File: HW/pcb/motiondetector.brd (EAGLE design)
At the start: 100 x 80 mm, 1 part, among them IC1 4000D

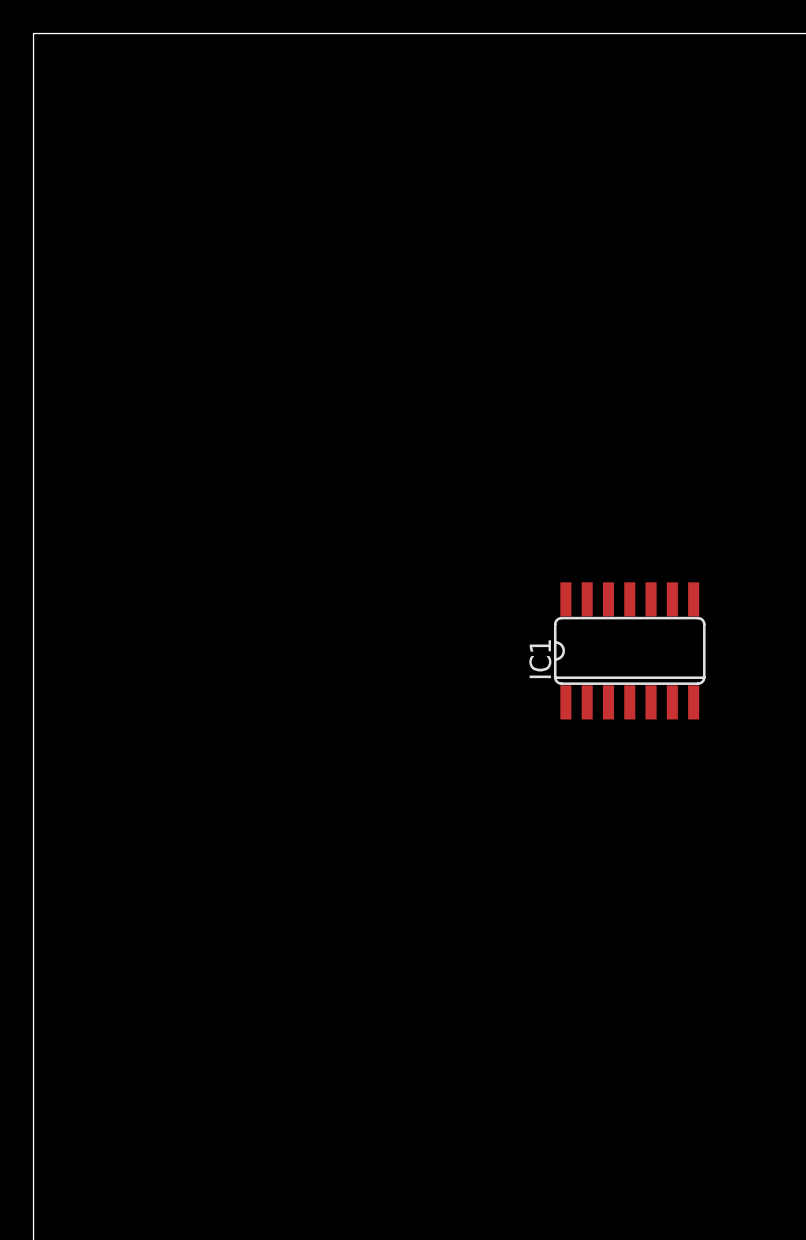
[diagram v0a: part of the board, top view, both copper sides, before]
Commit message: analog stage in circuit finished and testet
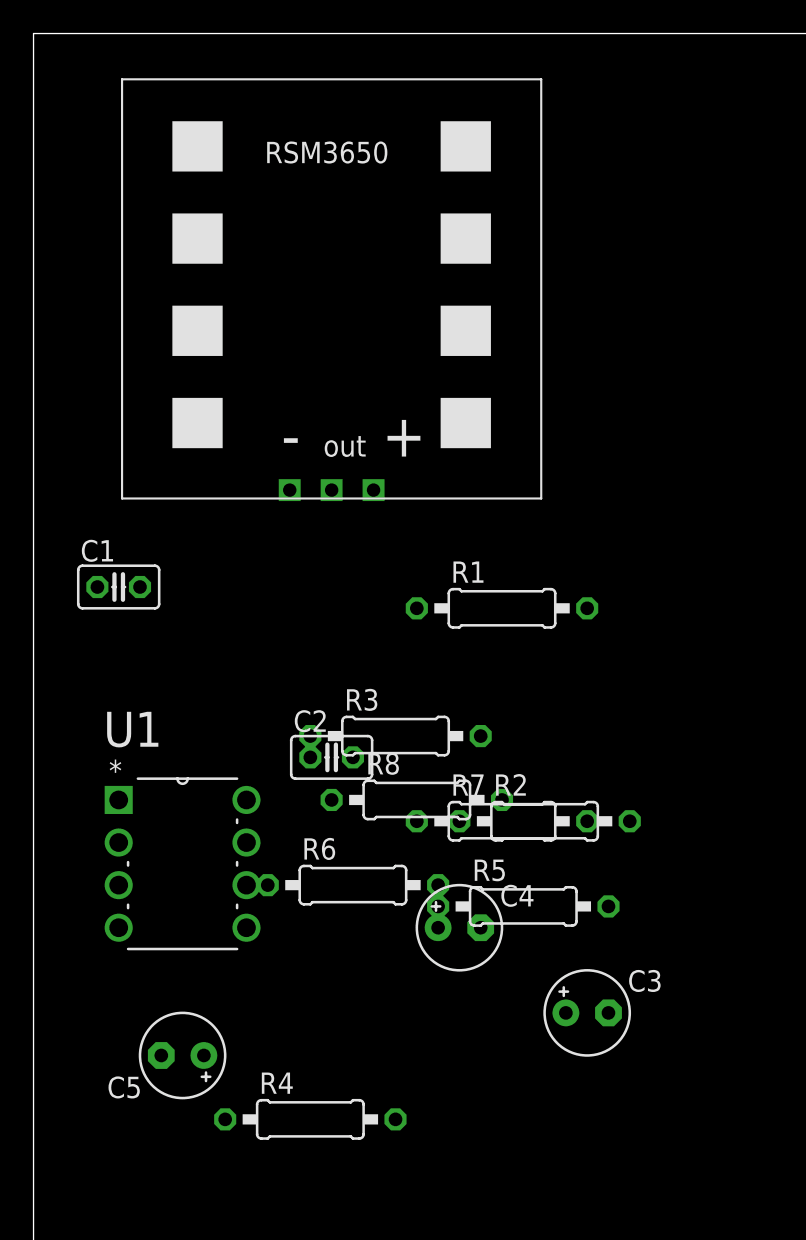
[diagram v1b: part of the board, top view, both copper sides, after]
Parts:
- removed IC1: 4000D, 40xx:SO14
- added C1, C2: 1nF, parts:C025-025X050
- added C3, C4, C5: 10uF, parts:E2,5-5
- added R1, R2: 4.7K, parts:0207/10
- added R3, R4: 1M, parts:0207/10
- added R5, R6: 1k, parts:0207/10
- added R7, R8: 150k, parts:0207/10
- added U$1: RSM3650, RSM3650:RSM3650
- added U1: LT1078CN8PBF, parts:DIP254P762X393-8
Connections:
- removed net VDD: IC1.14
- removed net VSS: IC1.7
- new net +3V3: R3.2, U$1.VCC, U1.8
- new net GND: C5.-, R4.1, U$1.VSS, U1.4
- new net N$1: C4.-, R1.1
- new net N$11: C2.1, R2.2, R8.1, U1.6
- new net N$2: C1.2, R1.2, R7.1, U1.2
- new net N$3: C4.+, U$1.OUT
- new net N$4: C3.-, R2.1
- new net N$5: R5.1
- new net N$6: R6.2, U1.3, U1.5
- new net N$7: C5.+, R3.1, R4.2, R6.1
- new net N$8: C2.2, R5.2, R8.2, U1.7
- new net N$9: C1.1, C3.+, R7.2, U1.1
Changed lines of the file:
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@@
 <layer number="97" name="Info" color="7" fill="1" visible="no" active="no"/>
 <layer number="98" name="Guide" color="6" fill="1" visible="no" active="no"/>
+<layer number="99" name="SpiceOrder" color="5" fill="1" visible="no" active="no"/>
 </layers>
 <board>
@@
 </autorouter>
 <elements>
-<element name="IC1" library="40xx" package="SO14" value="4000D" x="35.56" y="43.18"/>
+<element name="U1" library="parts" package="DIP254P762X393-8" value="LT1078CN8PBF" x="12.7" y="26.67">
+<attribute name="SUPPLIER" value="LINEAR TECHNOLOGY" x="12.7" y="26.67" size="1.778" layer="27" display="off"/>
+<attribute name="MPN" value="LT1078CN8#PBF" x="12.7" y="26.67" size="1.778" layer="27" display="off"/>
+<attribute name="OC_FARNELL" value="9559680" x="12.7" y="26.67" size="1.778" layer="27" display="off"/>
+<attribute name="OC_NEWARK" value="57M1404" x="12.7" y="26.67" size="1.778" layer="27" display="off"/>
+<attribute name="PACKAGE" value="PDIP" x="12.7" y="26.67" size="1.778" layer="27" display="off"/>
+</element>
+<element name="C1" library="parts" package="C025-025X050" value="1nF" x="5.08" y="46.99"/>
+<element name="C2" library="parts" package="C025-025X050" value="1nF" x="17.78" y="36.83"/>
+<element name="C3" library="parts" package="E2,5-5" value="10uF" x="33.02" y="21.59"/>
+<element name="C4" library="parts" package="E2,5-5" value="10uF" x="25.4" y="26.67"/>
+<element name="C5" library="parts" package="E2,5-5" value="10uF" x="8.89" y="19.05" rot="R180"/>
+<element name="R1" library="parts" package="0207/10" value="4.7K" x="27.94" y="45.72"/>
+<element name="R2" library="parts" package="0207/10" value="4.7K" x="30.48" y="33.02"/>
+<element name="R3" library="parts" package="0207/10" value="1M" x="21.59" y="38.1"/>
+<element name="R4" library="parts" package="0207/10" value="1M" x="16.51" y="15.24"/>
+<element name="R5" library="parts" package="0207/10" value="1k" x="29.21" y="27.94"/>
+<element name="R6" library="parts" package="0207/10" value="1k" x="19.05" y="29.21"/>
+<element name="R7" library="parts" package="0207/10" value="150k" x="27.94" y="33.02"/>
+<element name="R8" library="parts" package="0207/10" value="150k" x="22.86" y="34.29"/>
+<element name="U$1" library="RSM3650" package="RSM3650" value="RSM3650" x="17.78" y="64.77"/>
 </elements>
 <signals>
-<signal name="VSS">
-<contactref element="IC1" pad="7"/>
-</signal>
-<signal name="VDD">
-<contactref element="IC1" pad="14"/>
+<signal name="+3V3">
+<contactref element="U1" pad="8"/>
+<contactref element="R3" pad="2"/>
+<contactref element="U$1" pad="VCC"/>
+<wire x1="12.7" y1="34.29" x2="26.67" y2="38.1" width="0" layer="19" extent="1-1"/>
+<wire x1="20.28" y1="52.77" x2="12.7" y2="34.29" width="0" layer="19" extent="1-1"/>
+</signal>
+<signal name="N$1">
+<contactref element="C4" pad="-"/>
+<contactref element="R1" pad="1"/>
+<wire x1="26.67" y1="26.67" x2="22.86" y2="45.72" width="0" layer="19" extent="1-1"/>
+</signal>
+<signal name="N$2">
+<contactref element="R1" pad="2"/>
+<contactref element="U1" pad="2"/>
+<contactref element="R7" pad="1"/>
+<contactref element="C1" pad="2"/>
+<wire x1="33.02" y1="45.72" x2="22.86" y2="33.02" width="0" layer="19" extent="1-1"/>
+<wire x1="6.35" y1="46.99" x2="33.02" y2="45.72" width="0" layer="19" extent="1-1"/>
+<wire x1="5.08" y1="31.75" x2="6.35" y2="46.99" width="0" layer="19" extent="1-1"/>
+</signal>
+<signal name="N$4">
+<contactref element="C3" pad="-"/>
+<contactref element="R2" pad="1"/>
+<wire x1="34.29" y1="21.59" x2="25.4" y2="33.02" width="0" layer="19" extent="1-1"/>
+</signal>
+<signal name="N$6">
+<contactref element="U1" pad="3"/>
+<contactref element="U1" pad="5"/>
+<contactref element="R6" pad="2"/>
+<wire x1="12.7" y1="26.67" x2="24.13" y2="29.21" width="0" layer="19" extent="1-1"/>
+<wire x1="5.08" y1="29.21" x2="12.7" y2="26.67" width="0" layer="19" extent="1-1"/>
+</signal>
+<signal name="N$7">
+<contactref element="R3" pad="1"/>
+<contactref element="R4" pad="2"/>
+<contactref element="C5" pad="+"/>
+<contactref element="R6" pad="1"/>
+<wire x1="21.59" y1="15.24" x2="13.97" y2="29.21" width="0" layer="19" extent="1-1"/>
+<wire x1="16.51" y1="38.1" x2="21.59" y2="15.24" width="0" layer="19" extent="1-1"/>
+<wire x1="10.16" y1="19.05" x2="16.51" y2="38.1" width="0" layer="19" extent="1-1"/>
+</signal>
+<signal name="N$9">
+<contactref element="C1" pad="1"/>
+<contactref element="R7" pad="2"/>
+<contactref element="U1" pad="1"/>
+<contactref element="C3" pad="+"/>
+<wire x1="31.75" y1="21.59" x2="33.02" y2="33.02" width="0" layer="19" extent="1-1"/>
+<wire x1="3.81" y1="46.99" x2="31.75" y2="21.59" width="0" layer="19" extent="1-1"/>
+<wire x1="5.08" y1="34.29" x2="3.81" y2="46.99" width="0" layer="19" extent="1-1"/>
+</signal>
+<signal name="N$5">
+<contactref element="R5" pad="1"/>
+</signal>
+<signal name="GND">
+<contactref element="C5" pad="-"/>
+<contactref element="U1" pad="4"/>
+<contactref element="R4" pad="1"/>
+<contactref element="U$1" pad="VSS"/>
+<wire x1="7.62" y1="19.05" x2="11.43" y2="15.24" width="0" layer="19" extent="1-1"/>
+<wire x1="5.08" y1="26.67" x2="7.62" y2="19.05" width="0" layer="19" extent="1-1"/>
+<wire x1="15.28" y1="52.77" x2="5.08" y2="26.67" width="0" layer="19" extent="1-1"/>
+</signal>
+<signal name="N$8">
+<contactref element="R8" pad="2"/>
+<contactref element="C2" pad="2"/>
+<contactref element="U1" pad="7"/>
+<contactref element="R5" pad="2"/>
+<wire x1="34.29" y1="27.94" x2="27.94" y2="34.29" width="0" layer="19" extent="1-1"/>
+<wire x1="19.05" y1="36.83" x2="34.29" y2="27.94" width="0" layer="19" extent="1-1"/>
+<wire x1="12.7" y1="31.75" x2="19.05" y2="36.83" width="0" layer="19" extent="1-1"/>
+</signal>
+<signal name="N$11">
+<contactref element="R8" pad="1"/>
+<contactref element="C2" pad="1"/>
+<contactref element="R2" pad="2"/>
+<contactref element="U1" pad="6"/>
+<wire x1="35.56" y1="33.02" x2="17.78" y2="34.29" width="0" layer="19" extent="1-1"/>
+<wire x1="16.51" y1="36.83" x2="35.56" y2="33.02" width="0" layer="19" extent="1-1"/>
+<wire x1="12.7" y1="29.21" x2="16.51" y2="36.83" width="0" layer="19" extent="1-1"/>
+</signal>
+<signal name="N$3">
+<contactref element="U$1" pad="OUT"/>
+<contactref element="C4" pad="+"/>
+<wire x1="17.78" y1="52.77" x2="24.13" y2="26.67" width="0" layer="19" extent="1-1"/>
 </signal>
 </signals>

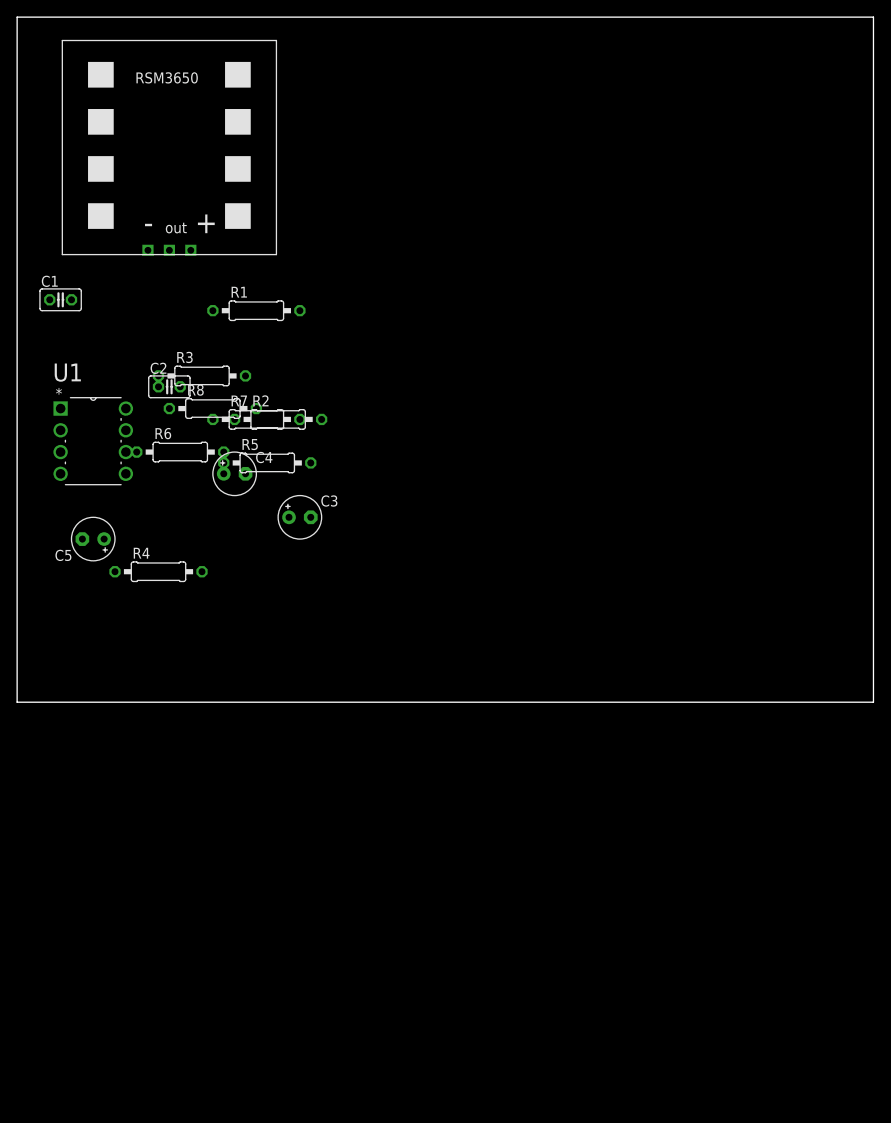
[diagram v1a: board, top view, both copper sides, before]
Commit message: base PIC24F circuit added
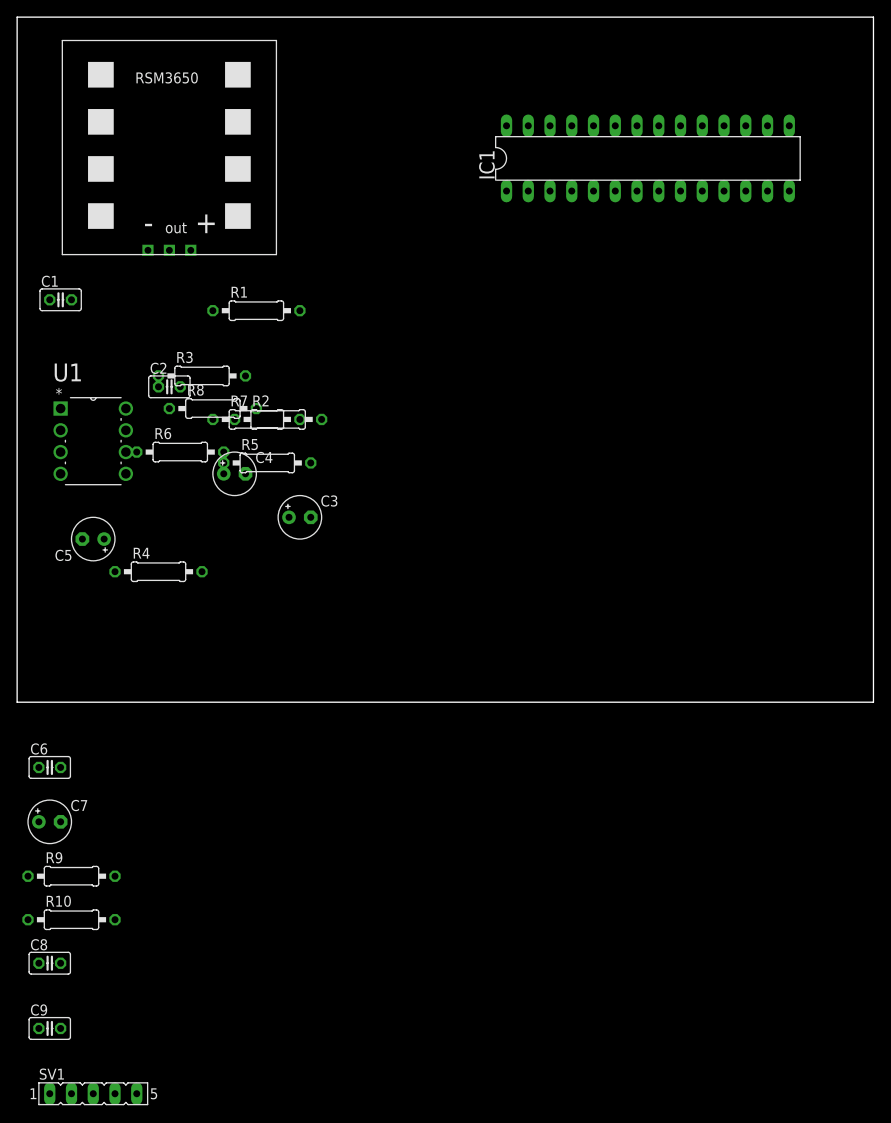
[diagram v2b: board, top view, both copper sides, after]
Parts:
- added C6, C8, C9: 100nF, parts:C025-025X050
- added C7: 10uF, parts:E2,5-5
- added IC1: PIC24FJ32GB002, PIC24FJXXGB0XX :DIL28-3
- added R10: 100R, parts:0207/10
- added R9: 10k, parts:0207/10
- added SV1: (no value), con-lsta:FE05-1
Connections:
- net N$5 renamed ROUT
- new net MCLR: C9.2, R10.2, R9.2, SV1.1
- new net N$12: C7.+, IC1.20
- new net N$13: IC1.1, R10.1
- new net PGEC1: IC1.5, SV1.5
- new net PGED1: IC1.4, SV1.4
- net +3V3: now also C6.2, C8.1, IC1.13, IC1.28, R9.1, SV1.2
- net GND: now also C6.1, C7.-, C8.2, C9.1, IC1.19, IC1.27, IC1.8, SV1.3
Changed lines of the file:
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@@
 <element name="R8" library="parts" package="0207/10" value="150k" x="22.86" y="34.29"/>
 <element name="U$1" library="RSM3650" package="RSM3650" value="RSM3650" x="17.78" y="64.77"/>
+<element name="IC1" library="PIC24FJXXGB0XX " package="DIL28-3" value="PIC24FJ32GB002" x="73.66" y="63.5"/>
+<element name="C6" library="parts" package="C025-025X050" value="100nF" x="3.81" y="-7.62"/>
+<element name="C7" library="parts" package="E2,5-5" value="10uF" x="3.81" y="-13.97"/>
+<element name="R9" library="parts" package="0207/10" value="10k" x="6.35" y="-20.32"/>
+<element name="R10" library="parts" package="0207/10" value="100R" x="6.35" y="-25.4"/>
+<element name="C8" library="parts" package="C025-025X050" value="100nF" x="3.81" y="-30.48"/>
+<element name="C9" library="parts" package="C025-025X050" value="100nF" x="3.81" y="-38.1"/>
+<element name="SV1" library="con-lsta" package="FE05-1" value="" x="8.89" y="-45.72">
+<attribute name="MPN" value="" x="8.89" y="-45.72" size="1.778" layer="27" display="off"/>
+<attribute name="MF" value="" x="8.89" y="-45.72" size="1.778" layer="27" display="off"/>
+<attribute name="OC_NEWARK" value="unknown" x="8.89" y="-45.72" size="1.778" layer="27" display="off"/>
+<attribute name="OC_FARNELL" value="unknown" x="8.89" y="-45.72" size="1.778" layer="27" display="off"/>
+</element>
 </elements>
 <signals>
@@
 <contactref element="R3" pad="2"/>
 <contactref element="U$1" pad="VCC"/>
+<contactref element="IC1" pad="28"/>
+<contactref element="C6" pad="2"/>
+<contactref element="R9" pad="1"/>
+<contactref element="IC1" pad="13"/>
+<contactref element="C8" pad="1"/>
+<contactref element="SV1" pad="2"/>
+<wire x1="57.15" y1="67.31" x2="87.63" y2="59.69" width="0" layer="19" extent="1-1"/>
+<wire x1="20.28" y1="52.77" x2="57.15" y2="67.31" width="0" layer="19" extent="1-1"/>
+<wire x1="26.67" y1="38.1" x2="20.28" y2="52.77" width="0" layer="19" extent="1-1"/>
 <wire x1="12.7" y1="34.29" x2="26.67" y2="38.1" width="0" layer="19" extent="1-1"/>
-<wire x1="20.28" y1="52.77" x2="12.7" y2="34.29" width="0" layer="19" extent="1-1"/>
+<wire x1="5.08" y1="-7.62" x2="12.7" y2="34.29" width="0" layer="19" extent="1-1"/>
+<wire x1="1.27" y1="-20.32" x2="5.08" y2="-7.62" width="0" layer="19" extent="1-1"/>
+<wire x1="2.54" y1="-30.48" x2="1.27" y2="-20.32" width="0" layer="19" extent="1-1"/>
+<wire x1="6.35" y1="-45.72" x2="2.54" y2="-30.48" width="0" layer="19" extent="1-1"/>
 </signal>
 <signal name="N$1">
@@
 <wire x1="5.08" y1="34.29" x2="3.81" y2="46.99" width="0" layer="19" extent="1-1"/>
 </signal>
-<signal name="N$5">
-<contactref element="R5" pad="1"/>
-</signal>
 <signal name="GND">
 <contactref element="C5" pad="-"/>
@@
 <contactref element="R4" pad="1"/>
 <contactref element="U$1" pad="VSS"/>
-<wire x1="7.62" y1="19.05" x2="11.43" y2="15.24" width="0" layer="19" extent="1-1"/>
-<wire x1="5.08" y1="26.67" x2="7.62" y2="19.05" width="0" layer="19" extent="1-1"/>
-<wire x1="15.28" y1="52.77" x2="5.08" y2="26.67" width="0" layer="19" extent="1-1"/>
+<contactref element="IC1" pad="27"/>
+<contactref element="C6" pad="1"/>
+<contactref element="C7" pad="-"/>
+<contactref element="IC1" pad="19"/>
+<contactref element="IC1" pad="8"/>
+<contactref element="C8" pad="2"/>
+<contactref element="C9" pad="1"/>
+<contactref element="SV1" pad="3"/>
+<wire x1="74.93" y1="59.69" x2="80.01" y2="67.31" width="0" layer="19" extent="1-1"/>
+<wire x1="59.69" y1="67.31" x2="74.93" y2="59.69" width="0" layer="19" extent="1-1"/>
+<wire x1="15.28" y1="52.77" x2="59.69" y2="67.31" width="0" layer="19" extent="1-1"/>
+<wire x1="5.08" y1="26.67" x2="15.28" y2="52.77" width="0" layer="19" extent="1-1"/>
+<wire x1="7.62" y1="19.05" x2="5.08" y2="26.67" width="0" layer="19" extent="1-1"/>
+<wire x1="11.43" y1="15.24" x2="7.62" y2="19.05" width="0" layer="19" extent="1-1"/>
+<wire x1="2.54" y1="-7.62" x2="11.43" y2="15.24" width="0" layer="19" extent="1-1"/>
+<wire x1="5.08" y1="-13.97" x2="2.54" y2="-7.62" width="0" layer="19" extent="1-1"/>
+<wire x1="5.08" y1="-30.48" x2="5.08" y2="-13.97" width="0" layer="19" extent="1-1"/>
+<wire x1="2.54" y1="-38.1" x2="5.08" y2="-30.48" width="0" layer="19" extent="1-1"/>
+<wire x1="8.89" y1="-45.72" x2="2.54" y2="-38.1" width="0" layer="19" extent="1-1"/>
 </signal>
 <signal name="N$8">
@@
 <wire x1="17.78" y1="52.77" x2="24.13" y2="26.67" width="0" layer="19" extent="1-1"/>
 </signal>
+<signal name="ROUT">
+<contactref element="R5" pad="1"/>
+</signal>
+<signal name="N$12">
+<contactref element="IC1" pad="20"/>
+<contactref element="C7" pad="+"/>
+<wire x1="2.54" y1="-13.97" x2="77.47" y2="67.31" width="0" layer="19" extent="1-1"/>
+</signal>
+<signal name="MCLR">
+<contactref element="R9" pad="2"/>
+<contactref element="R10" pad="2"/>
+<contactref element="C9" pad="2"/>
+<contactref element="SV1" pad="1"/>
+<wire x1="5.08" y1="-38.1" x2="3.81" y2="-45.72" width="0" layer="19" extent="1-1"/>
+<wire x1="11.43" y1="-25.4" x2="5.08" y2="-38.1" width="0" layer="19" extent="1-1"/>
+<wire x1="11.43" y1="-20.32" x2="11.43" y2="-25.4" width="0" layer="19" extent="1-1"/>
+</signal>
+<signal name="N$13">
+<contactref element="R10" pad="1"/>
+<contactref element="IC1" pad="1"/>
+<wire x1="1.27" y1="-25.4" x2="57.15" y2="59.69" width="0" layer="19" extent="1-1"/>
+</signal>
+<signal name="PGED1">
+<contactref element="IC1" pad="4"/>
+<contactref element="SV1" pad="4"/>
+<wire x1="11.43" y1="-45.72" x2="64.77" y2="59.69" width="0" layer="19" extent="1-1"/>
+</signal>
+<signal name="PGEC1">
+<contactref element="IC1" pad="5"/>
+<contactref element="SV1" pad="5"/>
+<wire x1="13.97" y1="-45.72" x2="67.31" y2="59.69" width="0" layer="19" extent="1-1"/>
+</signal>
 </signals>
